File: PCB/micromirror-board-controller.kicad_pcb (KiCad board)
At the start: 2 copper layers, 74 x 80 mm, 24 parts, among them J1 Barrel_Jack, J2 Conn_01x04_Female, J3 Conn_01x03_Female, J4 Conn_2Rows-51Pins, J6 USB_C_Receptacle_USB2.0, SW1 SW_Push, SW2 SW_Push, U1 Pico, U2 LM1117IMPX-5.0

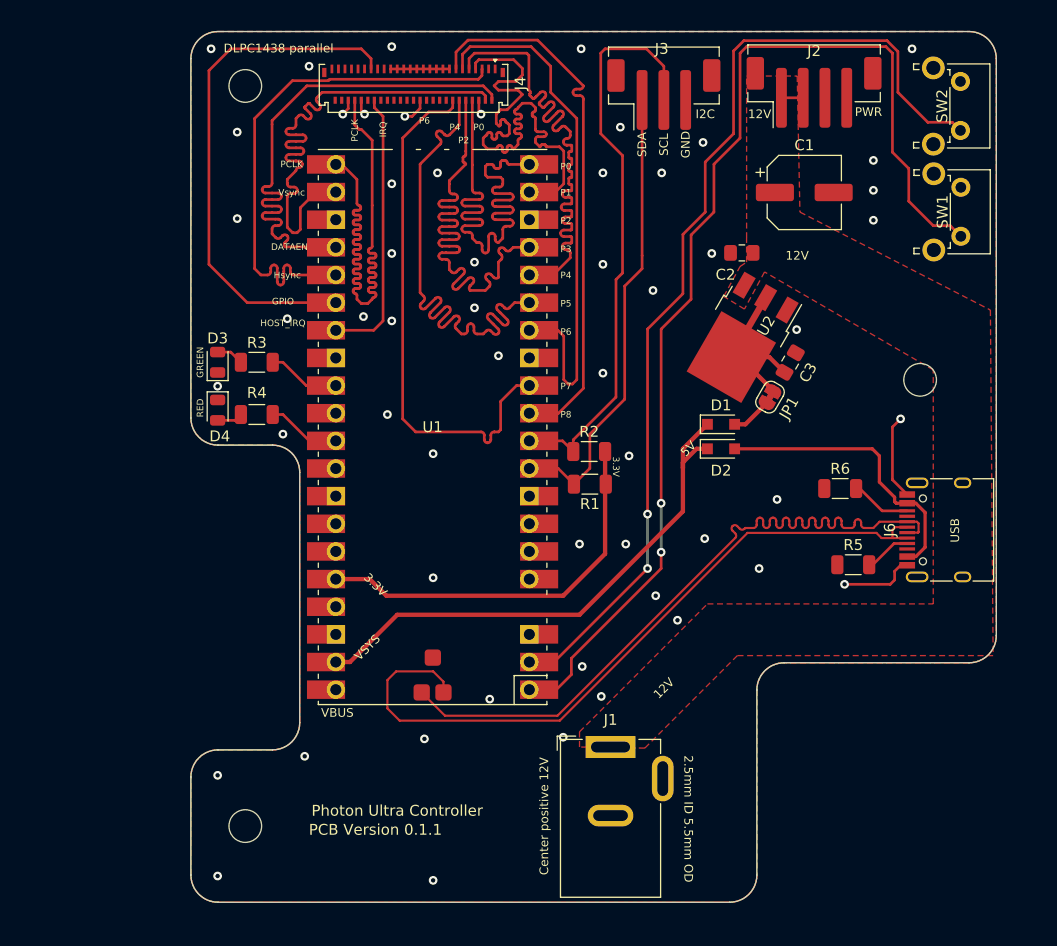
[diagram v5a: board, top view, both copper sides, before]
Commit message: Add licence
Add software and hardware licence. Added open hardware and licence info to PCB.
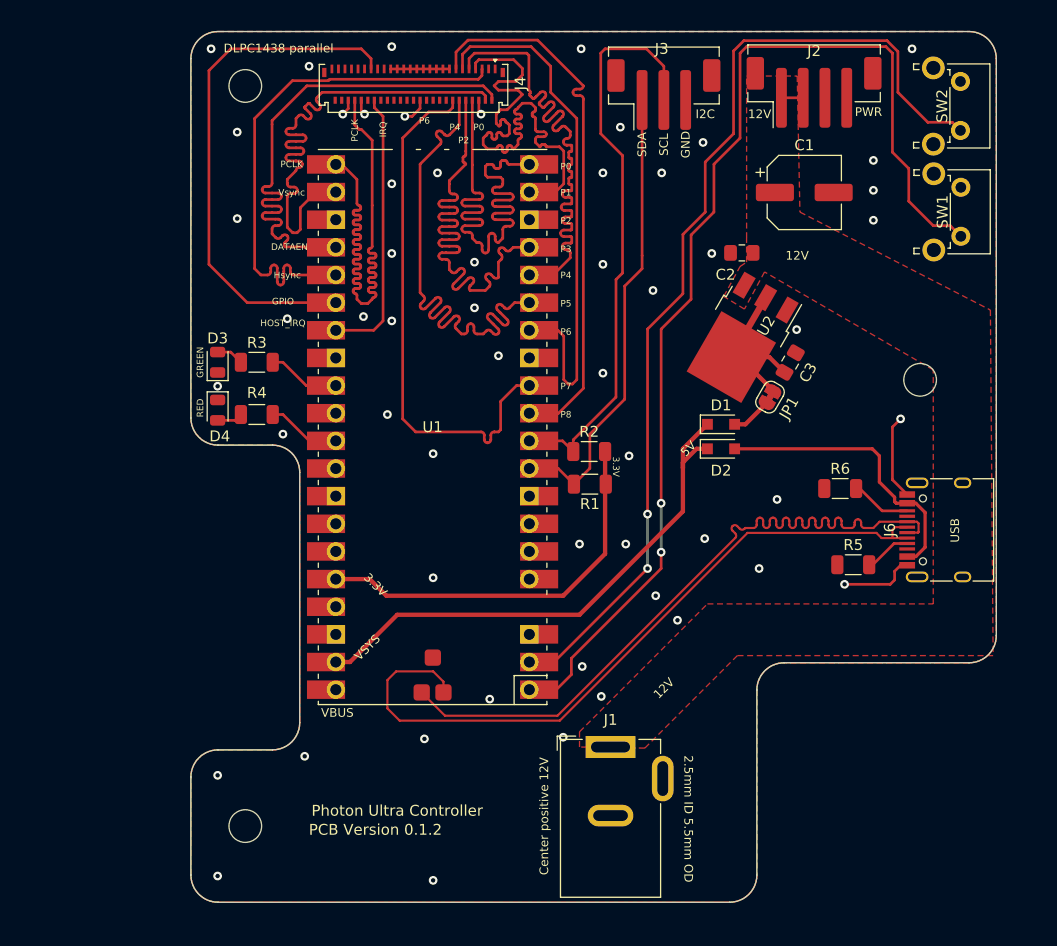
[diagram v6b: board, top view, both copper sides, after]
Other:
- board text added: "CERN-OHL-W-2.0"
- board text added: "Licenced under"
- board text added: "PCB Version 0.1.2"
- board text removed: "PCB Version 0.1.1"

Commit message: Improved USB lines connectivity
Fixed the tricky blind SMD pad approach with cutout and backside wire connection. Added some 3D models for all board components. Reworked some silkscreen. Added a TX/RX serial connector for convenience
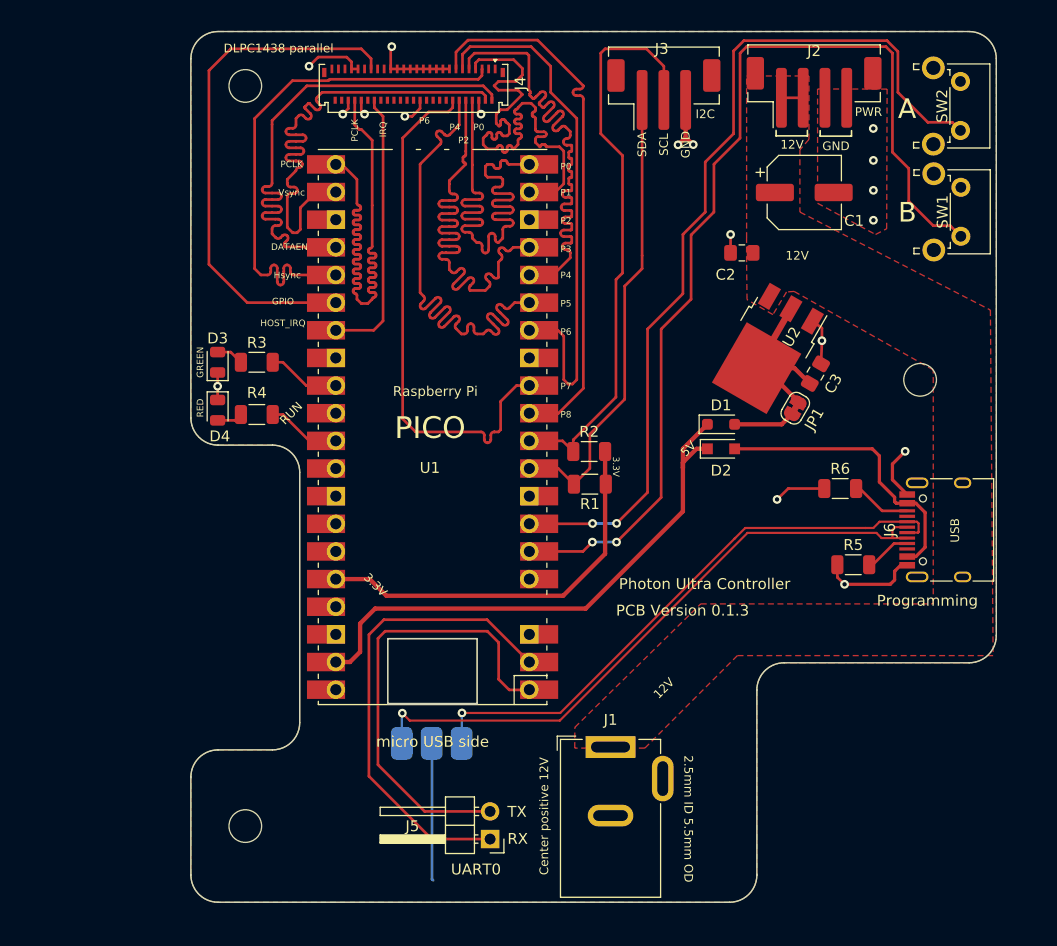
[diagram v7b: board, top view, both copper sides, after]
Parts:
- added J5: Conn_01x02_Pin, Connector_PinHeader_2.54mm:PinHeader_1x02_P2.54mm_Horizontal, F.Cu at (143.0, 131.6)
- added U3: ~, photon-ultra-board:usb-handsolder-pads, B.Cu at (137.7, 122.8)
- U1: footprint MCU_RaspberryPi_and_Boards:RPi_Pico_SMD_for-photon-ultra -> photon-ultra-board:RPi_Pico_SMD_TH
- moved JP1 2.54 mm to (171.1, 92.0)
- moved U2 2.54 mm to (168.6, 86.5)
- moved C3 2.54 mm to (172.9, 88.8)
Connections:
- J6 pad A6: /D- -> /D+
- J6 pad A7: /D+ -> /D-
- J6 pad B6: /D- -> /D+
- J6 pad B7: /D+ -> /D-
- SW1 pad 2: Net-(SW1-Pad2) -> Switch B
- SW2 pad 2: Net-(SW2-Pad2) -> Switch A
- U1 pad 1: Net-(SW1-Pad2) -> /TX
- U1 pad 2: Net-(SW2-Pad2) -> /RX
- U1 pad 6: unconnected-(U1-Pad6) -> Switch B
- U1 pad 7: unconnected-(U1-Pad7) -> Switch A
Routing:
- net Net-(SW1-Pad2): track 102.8 -> 0.00 mm, vias 2 -> 0
- net Switch B: track 0.00 -> 92.8 mm, vias 0 -> 2
- net Net-(SW2-Pad2): track 92.1 -> 0.00 mm, vias 2 -> 0
- net Switch A: track 0.00 -> 82.7 mm, vias 0 -> 2
- net /RX: track 0.00 -> 43.4 mm
- net /TX: track 0.00 -> 42.1 mm
- net GND: track 26.9 -> 65.2 mm, vias 56 -> 18
- net /D+: track 67.3 -> 54.1 mm, vias 0 -> 1
- net /D-: track 67.6 -> 59.0 mm, vias 0 -> 1
- net /+5V: track 20.7 -> 22.6 mm
- net /+5V VSYS: track 49.8 -> 51.3 mm
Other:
- outline, holes or cut-outs redrawn
- board text added: "A"
- board text added: "B"
- board text added: "Designed by Nemo Andrea"
- board text added: "PCB Version 0.1.3"
- board text added: "Programming"
- board text added: "RX"
- board text added: "TX"
- board text added: "UART0"
- board text removed: "PCB Version 0.1.2"

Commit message: Fix +12V pinout and revise board
Fixed the 12V board pinout (apparently GND and VSUP are swapped).  Some early code on talking to the DLPC1438; not all verified to be correct yet.
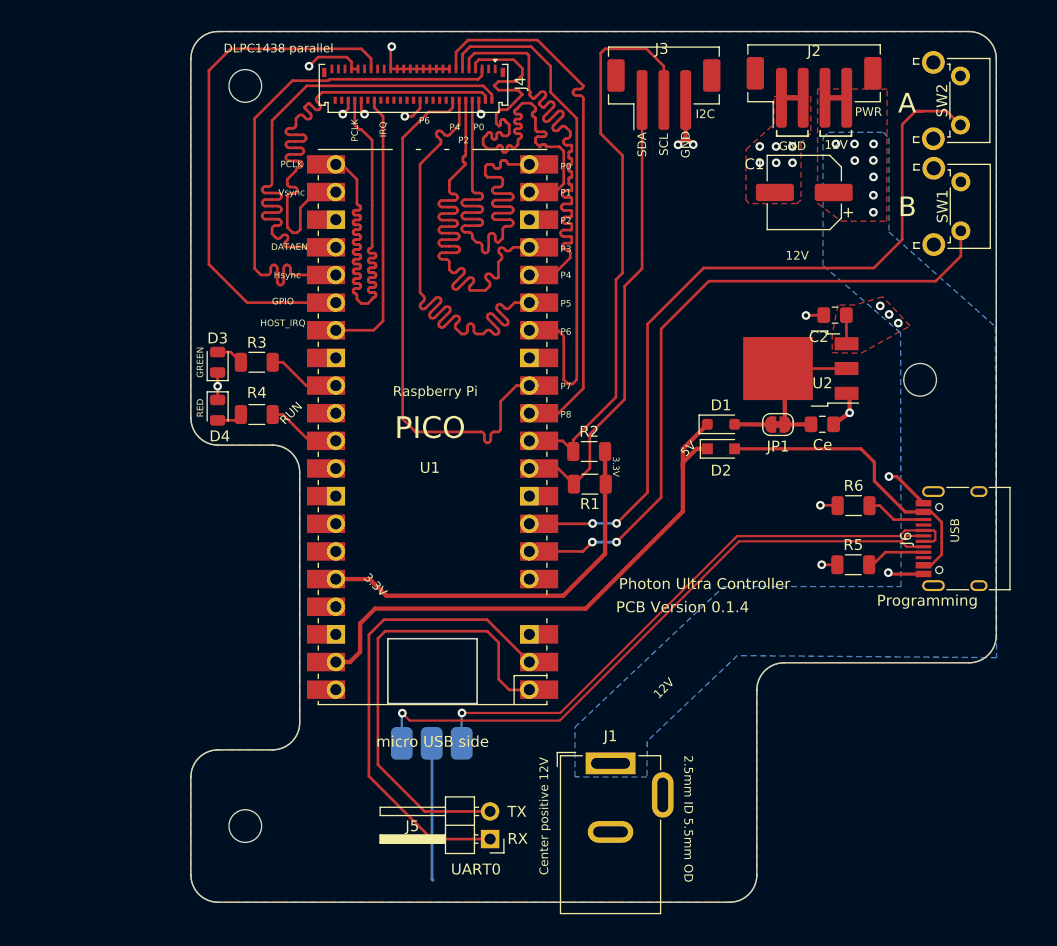
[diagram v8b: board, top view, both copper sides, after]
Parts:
- moved C2 10.3 mm to (174.7, 83.5)
- moved Ce 4.70 mm to (173.6, 93.5), turned to 0 degrees
- moved U2 3.54 mm to (171.6, 88.4), turned to 180 degrees
- moved JP1 2.19 mm to (169.5, 93.5), turned to 0 degrees
- moved R6 1.99 mm to (176.4, 101.0)
- moved J6 1.70 mm to (186.9, 104.0)
- moved J1 1.50 mm to (154.1, 124.7)
- moved SW1 0.50 mm to (186.3, 71.2)
- moved SW2 0.50 mm to (186.2, 61.5)
- turned C1 to 180 degrees
- renumbered C3 to Ce
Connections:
- net /GPIO 9 renamed /PROJ_ON
- J2 pad 1: /+12V -> GND
- J2 pad 2: /+12V -> GND
- J2 pad 3: GND -> /+12V
- J2 pad 4: GND -> /+12V
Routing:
- net Switch B: track 92.8 -> 62.3 mm
- net Switch A: track 82.7 -> 71.6 mm
- net GND: track 65.2 -> 58.4 mm, vias 18 -> 21
- net /+5V: track 22.6 -> 17.2 mm
- net /+12V: track 2.00 -> 4.63 mm, vias 0 -> 11
- net /D-: track 59.0 -> 60.3 mm
- net Net-(J6-CC1): track 4.30 -> 5.47 mm
- net /VBUS-C: track 26.8 -> 27.9 mm
- net /D+: track 54.1 -> 55.2 mm
- added copper zone on B.Cu, net /+12V
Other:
- board text added: "PCB Version 0.1.4"
- board text removed: "PCB Version 0.1.3"
